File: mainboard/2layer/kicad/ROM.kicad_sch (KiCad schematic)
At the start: 29 parts, among them U1 MMN2716, U18 MMN2716, U23 MMN2716, U42 MMN2716, U59 MMN2716, U70 74LS42, U75 MMN2716, U84 MMN2716, U89 27C128, U91 MMN2716

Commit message: some cleanup
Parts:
- added U93: 27C512, Package_DIP:DIP-28_W15.24mm, symbol Memory_EPROM:27C512
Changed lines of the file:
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@@
+    )
+  )
+  (symbol (lib_id "Memory_EPROM:27C512") (at 215.265 165.1 0) (unit 1)
+    (in_bom yes) (on_board yes) (dnp no) (fields_autoplaced)
+    (property "Reference" "U93" (at 217.4591 134.62 0)
+      (effects (font (size 1.27 1.27)) (justify left))
+    )
+    (property "Value" "27C512" (at 217.4591 137.16 0)
+      (effects (font (size 1.27 1.27)) (justify left))
+    )
+    (property "Footprint" "Package_DIP:DIP-28_W15.24mm" (at 215.265 165.1 0)
+      (effects (font (size 1.27 1.27)) hide)
+    )
+    (property "Datasheet" "http://ww1.microchip.com/downloads/en/DeviceDoc/doc0015.pdf" (at 215.265 165.1 0)
+      (effects (font (size 1.27 1.27)) hide)
+    )
+    (pin "1")
+    (pin "10")
+    (pin "11")
+    (pin "12")
+    (pin "13")
+    (pin "14")
+    (pin "15")
+    (pin "16")
+    (pin "17")
+    (pin "18")
+    (pin "19")
+    (pin "2")
+    (pin "20")
+    (pin "21")
+    (pin "22")
+    (pin "23")
+    (pin "24")
+    (pin "25")
+    (pin "26")
+    (pin "27")
+    (pin "28")
+    (pin "3")
+    (pin "4")
+    (pin "5")
+    (pin "6")
+    (pin "7")
+    (pin "8")
+    (pin "9")
+    (instances
+      (project "main"
+        (path "/ae158d42-76cc-4911-a621-4cc28931c98b/00000000-0000-0000-0000-00006301c001"
+          (reference "U93") (unit 1)
+        )
+      )
     )
   )

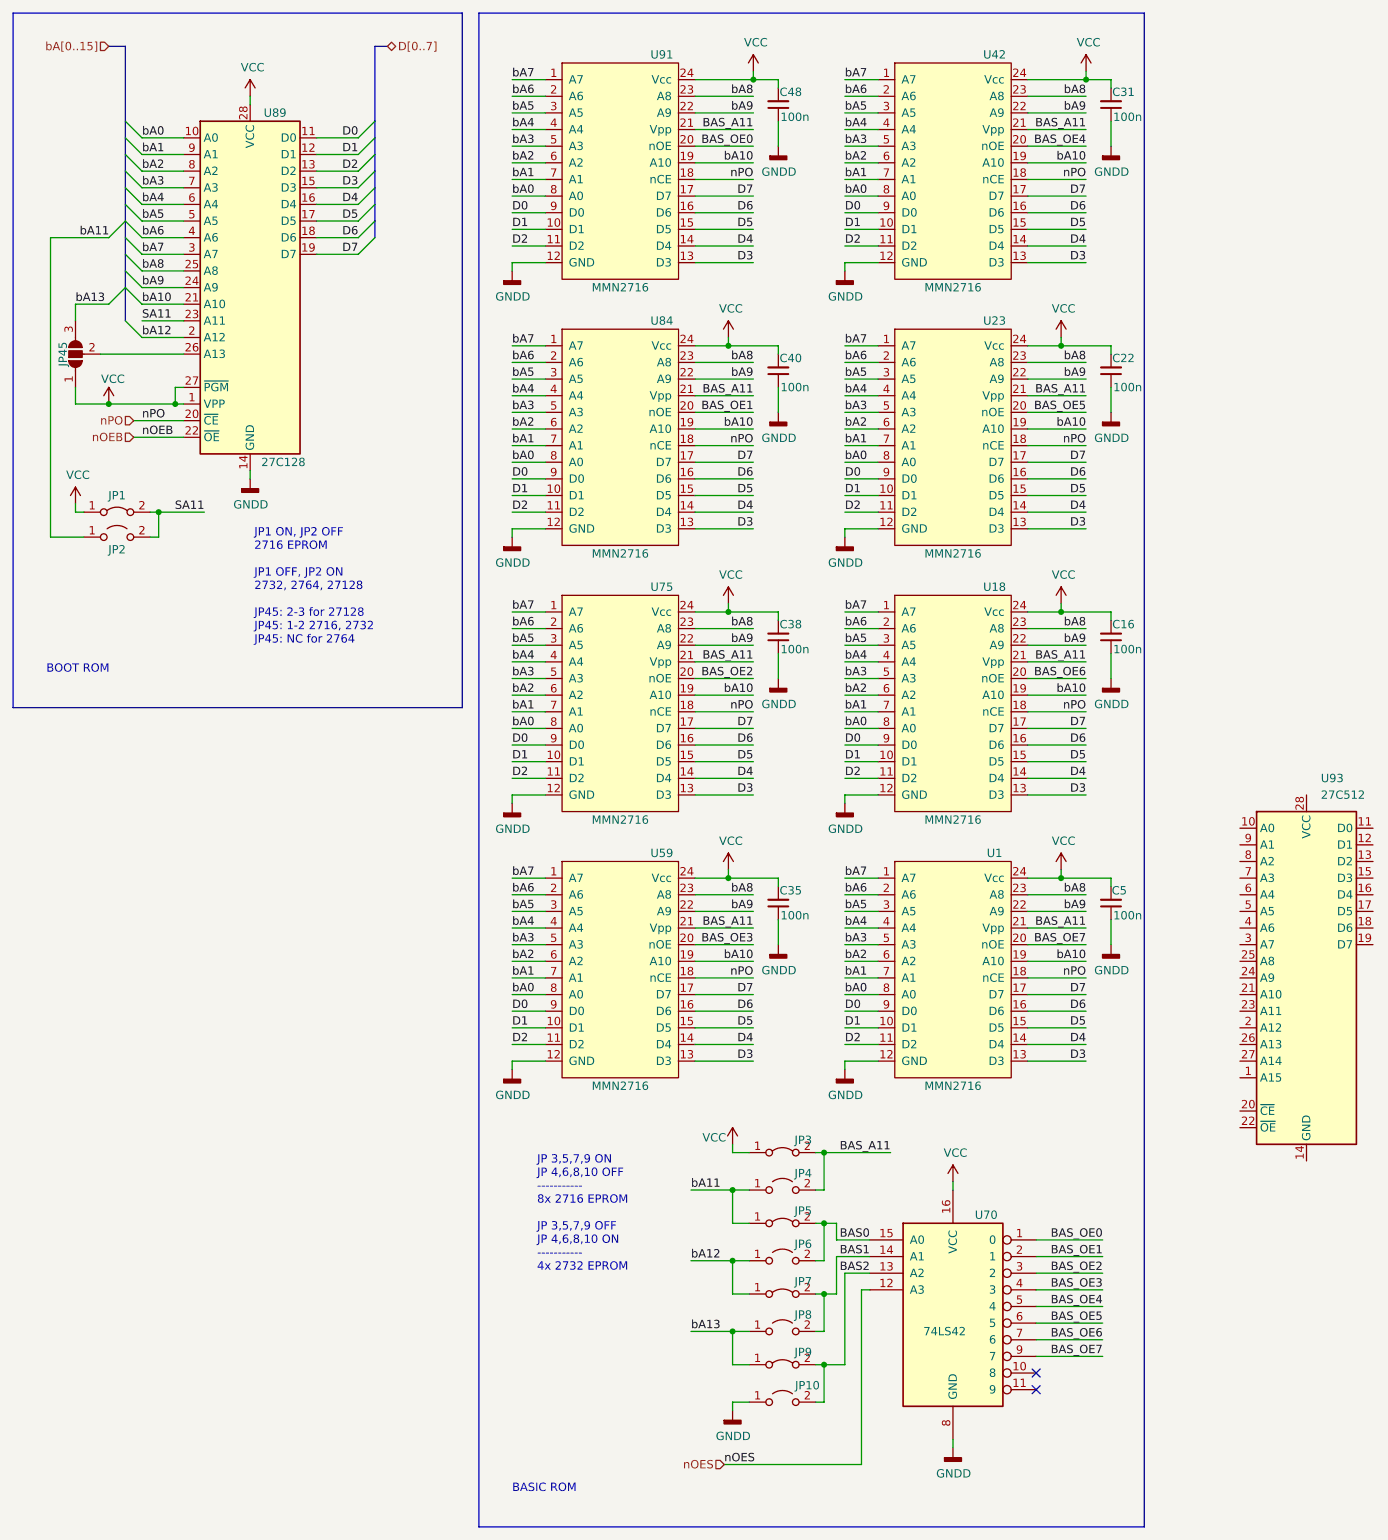
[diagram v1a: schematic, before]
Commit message: update to latest changes in mainboard schematic
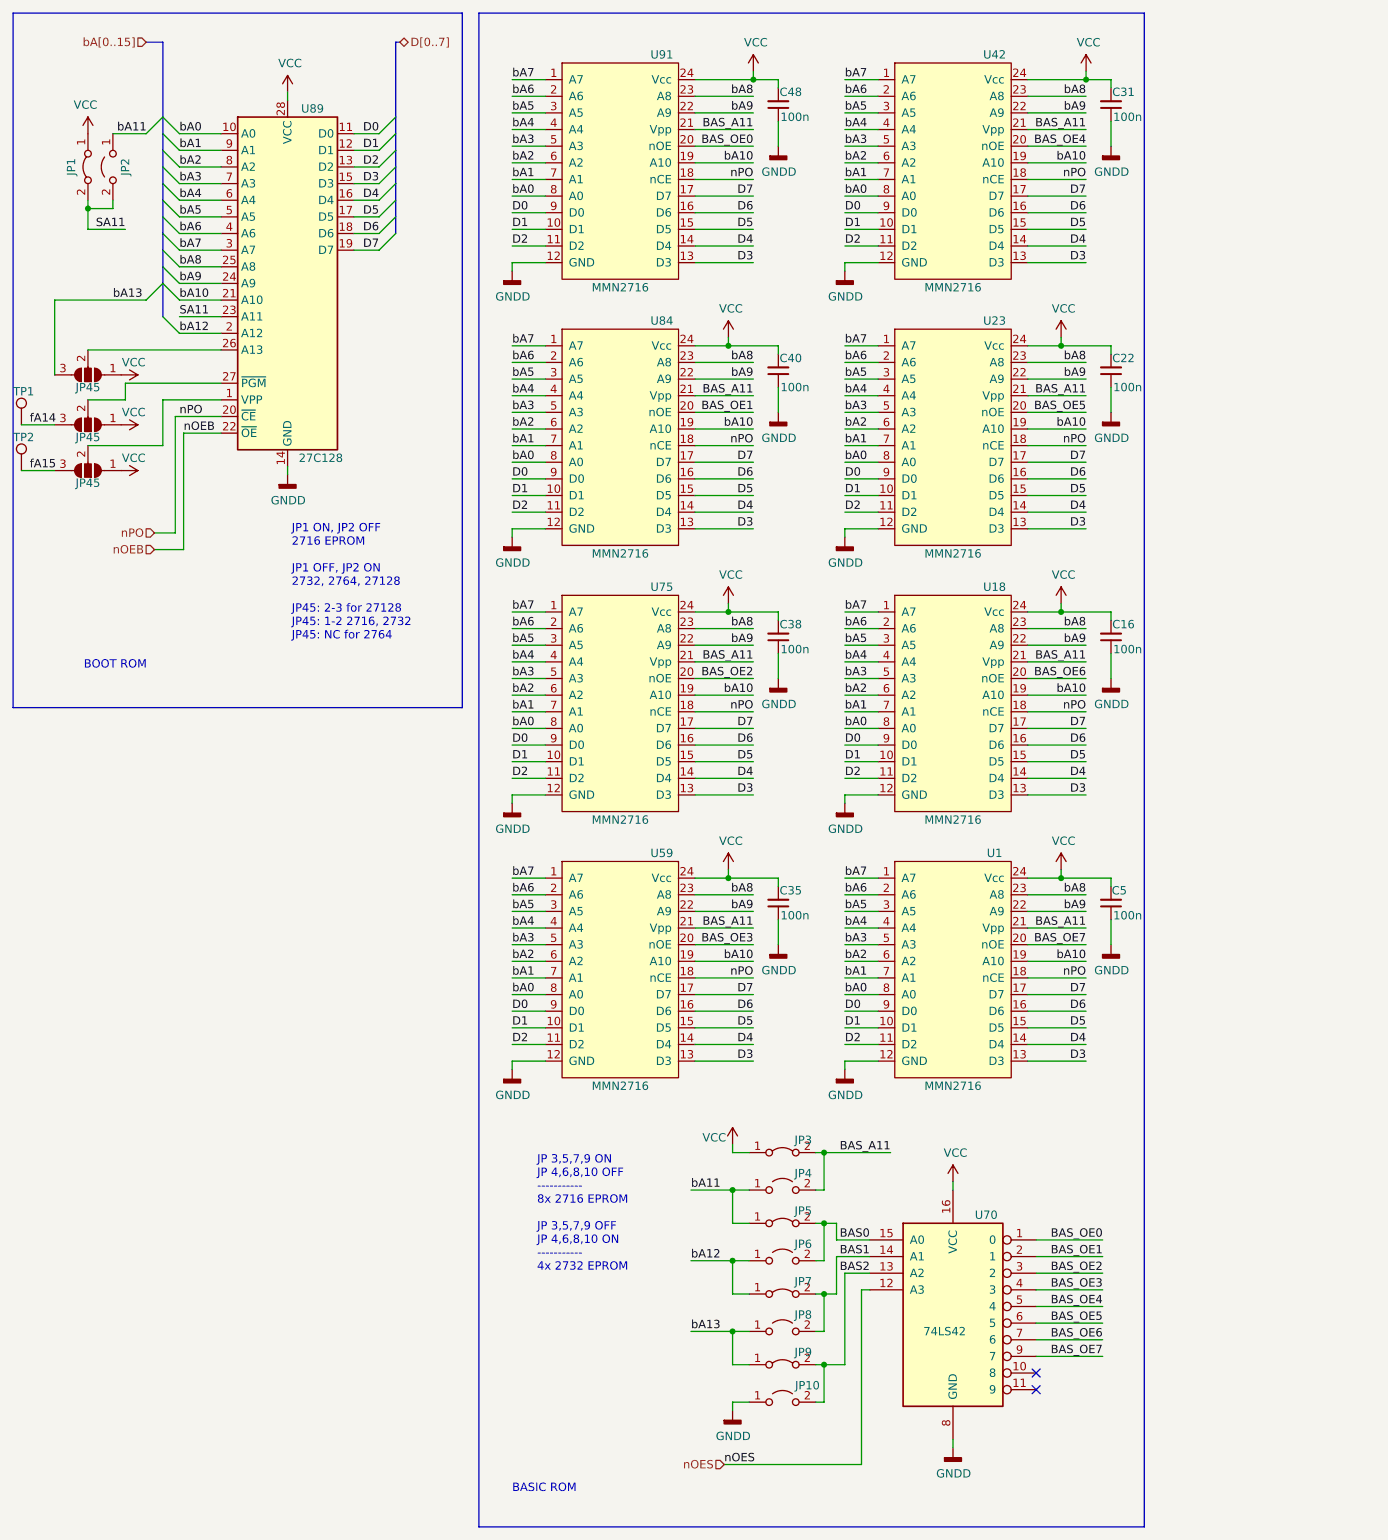
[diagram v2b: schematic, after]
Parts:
- removed U93: 27C512, Package_DIP:DIP-28_W15.24mm, symbol Memory_EPROM:27C512
- added JP45 (x2): SolderJumper_3_Open, Jumper:SolderJumper-3_P1.3mm_Open_Pad1.0x1.5mm, symbol Jumper:SolderJumper_3_Open
- added TP1, TP2: ~, TestPoint:TestPoint_THTPad_1.5x1.5mm_Drill0.7mm, symbol Connector:TestPoint
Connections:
- net VCC: now also JP45.1 (A), JP45.1 (A); no longer U89.1 (VPP), U89.27 (~{PGM})
- new net: JP45.2 (C), U89.1 (VPP)
- new net: JP45.2 (C), U89.27 (~{PGM})
- new net fA14: JP45.3 (B), TP1.1
- new net fA15: JP45.3 (B), TP2.1
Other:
- moved on the sheet: JP1, JP2, JP45, U89
